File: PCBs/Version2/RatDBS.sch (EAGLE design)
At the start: 18 parts

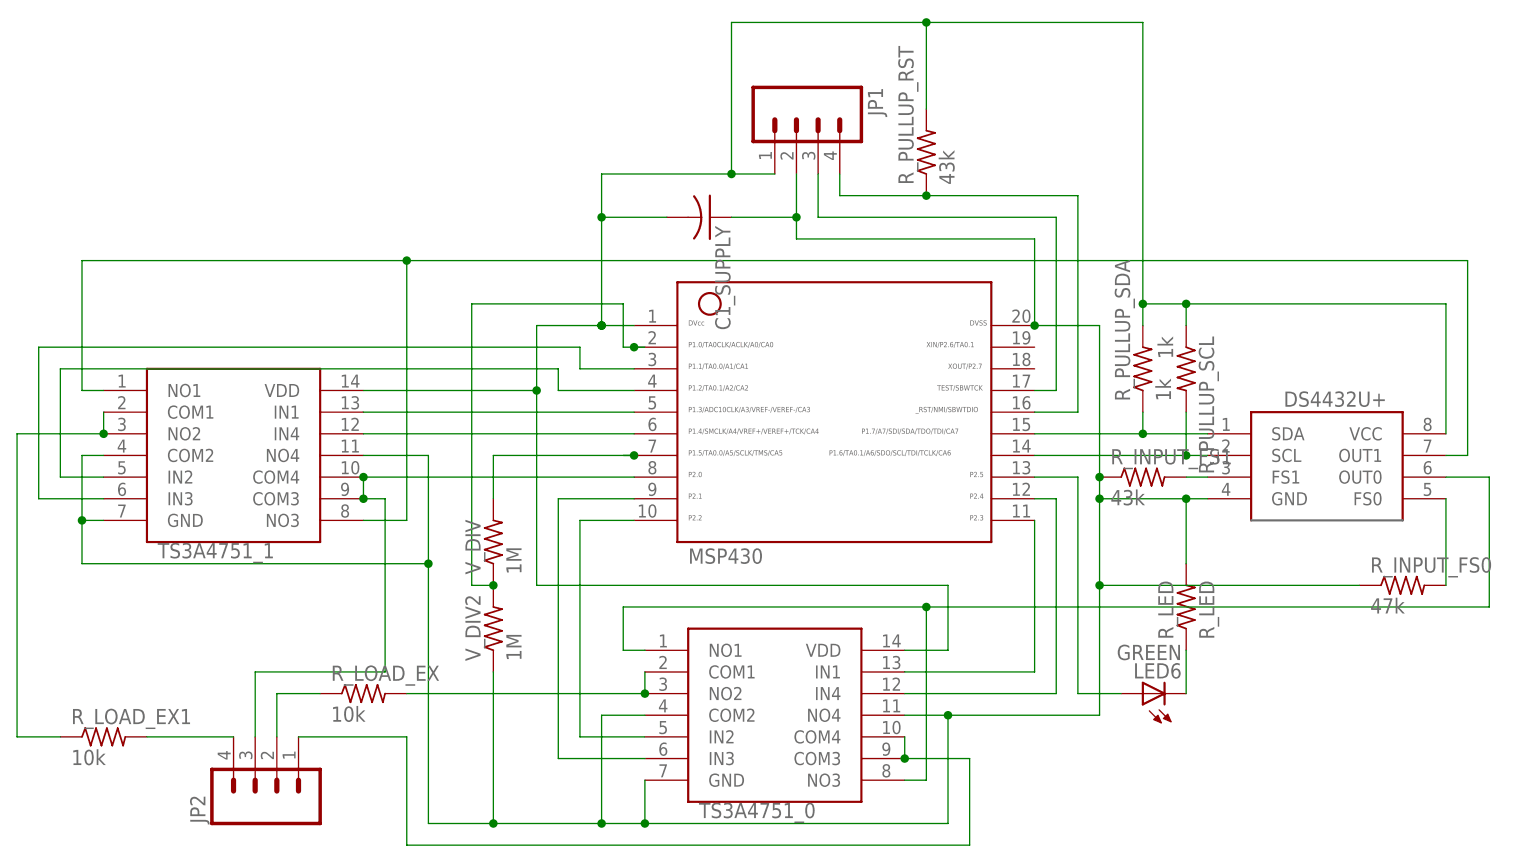
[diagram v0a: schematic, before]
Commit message: Added single channel stimulator
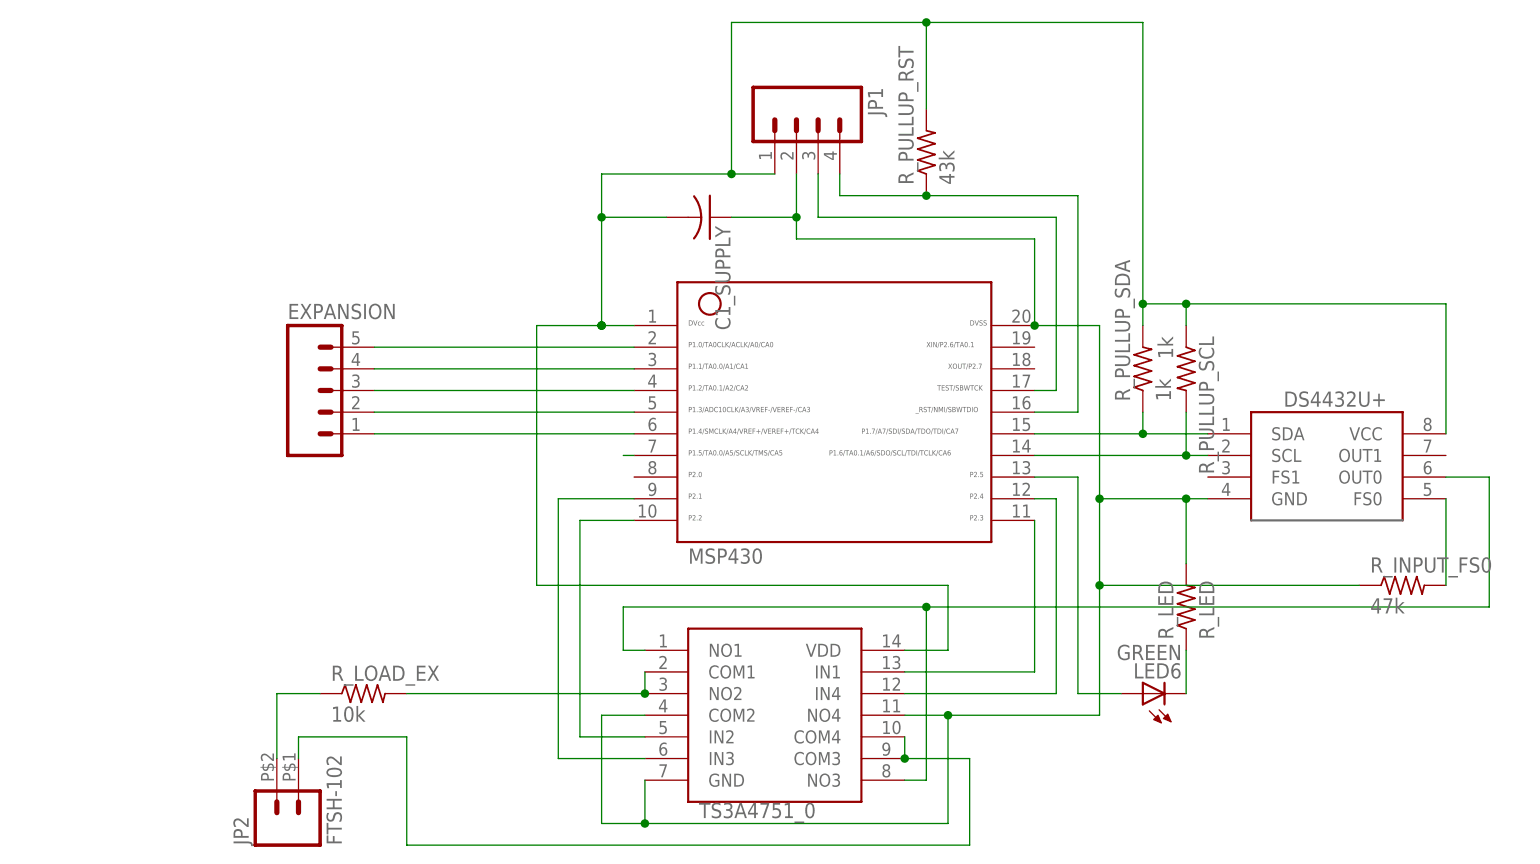
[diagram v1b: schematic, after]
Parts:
- removed R_INPUT_FS1: 43k, BiphasicBoard:R-US_R0603
- removed R_LOAD_EX1: 10k, BiphasicBoard:R-US_R0603
- removed TS3A4751_1: (no value), BiphasicBoard:TS3A4751
- removed V_DIV, V_DIV2: 1M, BiphasicBoard:R-US_R0603
- added EXPANSION: (no value), SparkFun:M051.27MM
- JP2: value (none) -> FTSH-102; device SparkFun:M041.27MM -> Samtec50Mil:FTSH-102
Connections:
- removed net DAC_OUT1: DS4432U+.OUT1, TS3A4751_1.NO1, TS3A4751_1.NO3
- removed net IN1_1: MSP430.5, TS3A4751_1.IN1
- removed net IN2_1: MSP430.4, TS3A4751_1.IN2
- removed net IN3_1: MSP430.3, TS3A4751_1.IN3
- removed net IN4_1: MSP430.6, TS3A4751_1.IN4
- removed net LOAD1_1: R_LOAD_EX1.1, TS3A4751_1.COM1, TS3A4751_1.NO2
- removed net LOAD2_1: JP2.3, MSP430.8, TS3A4751_1.COM3, TS3A4751_1.COM4
- removed net VIA1: DS4432U+.FS1, R_INPUT_FS1.2
- new net N$10: EXPANSION.3, MSP430.4
- new net N$11: EXPANSION.4, MSP430.3
- new net N$12: EXPANSION.5, MSP430.2
- net GND: no longer R_INPUT_FS1.1, TS3A4751_1.COM2, TS3A4751_1.GND, TS3A4751_1.NO4, V_DIV2.1
- net N$3: now also EXPANSION.1, MSP430.6; no longer JP2.4, R_LOAD_EX1.2
- net N$6: no longer V_DIV.2
- net N$7: now also EXPANSION.2, MSP430.5; no longer MSP430.2, V_DIV.1, V_DIV2.2
- net VDD: no longer TS3A4751_1.VDD

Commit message: Changed some colors and labels, changed code directory structure, and added docs for RF430
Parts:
- C1_SUPPLY: value (none) -> 10uF
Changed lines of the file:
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@@
 <?xml version="1.0" encoding="utf-8"?>
 <!DOCTYPE eagle SYSTEM "eagle.dtd">
-<eagle version="6.5.0">
+<eagle version="7.3.0">
 <drawing>
 <settings>
@@
 <part name="MSP430" library="BiphasicBoard" deviceset="MSP430" device=""/>
 <part name="TS3A4751_0" library="BiphasicBoard" deviceset="TS3A4751" device=""/>
-<part name="C1_SUPPLY" library="resistor" deviceset="C-US" device="C0603"/>
+<part name="C1_SUPPLY" library="resistor" deviceset="C-US" device="C0603" value="10uF"/>
 <part name="LED6" library="SparkFun-LED" deviceset="LED" device="1206" value="GREEN"/>
 <part name="R_LOAD_EX" library="BiphasicBoard" deviceset="R-US_" device="R0603" value="10k"/>
